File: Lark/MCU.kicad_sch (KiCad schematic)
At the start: 19 parts, among them J9 0530470410, U14 STM32H743VIT6, Y1 8Mhz

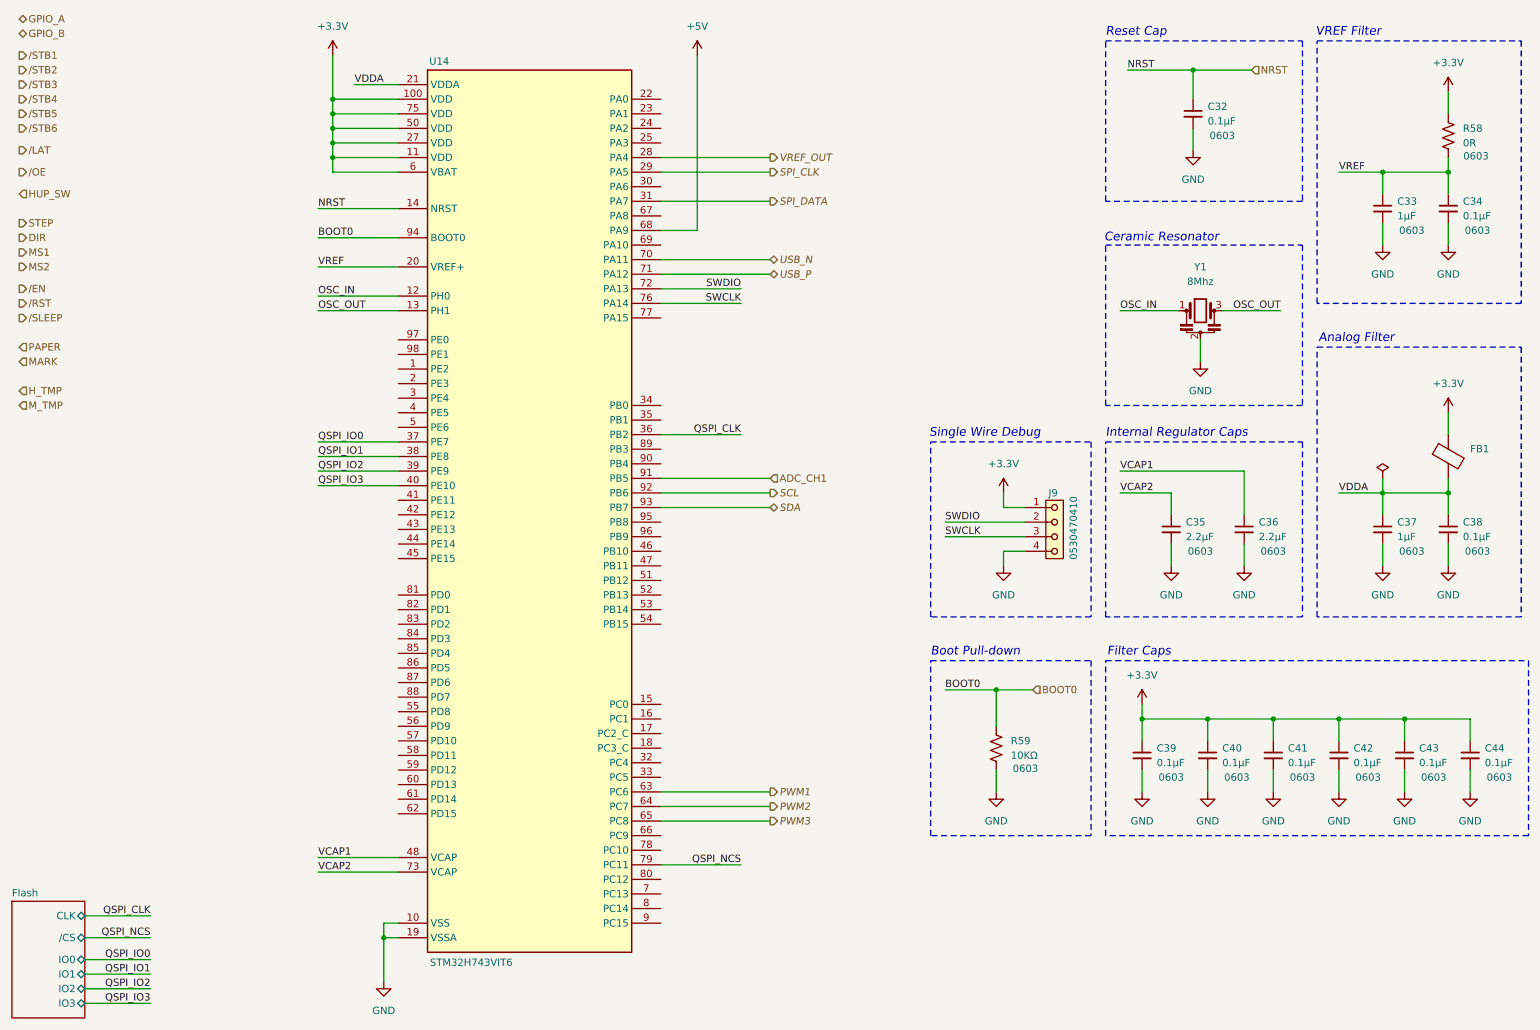
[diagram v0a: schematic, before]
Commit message: updated WIP
- fixed high-side switch (swapped out pfets)
- swapped out bleeder fet.
- changed a few footprints.
- changed zeners to 15v ones
- added soft-start cap back in to the high-side switch.

(today ive mainly been struggling with the inrush current, but I think its solved now)
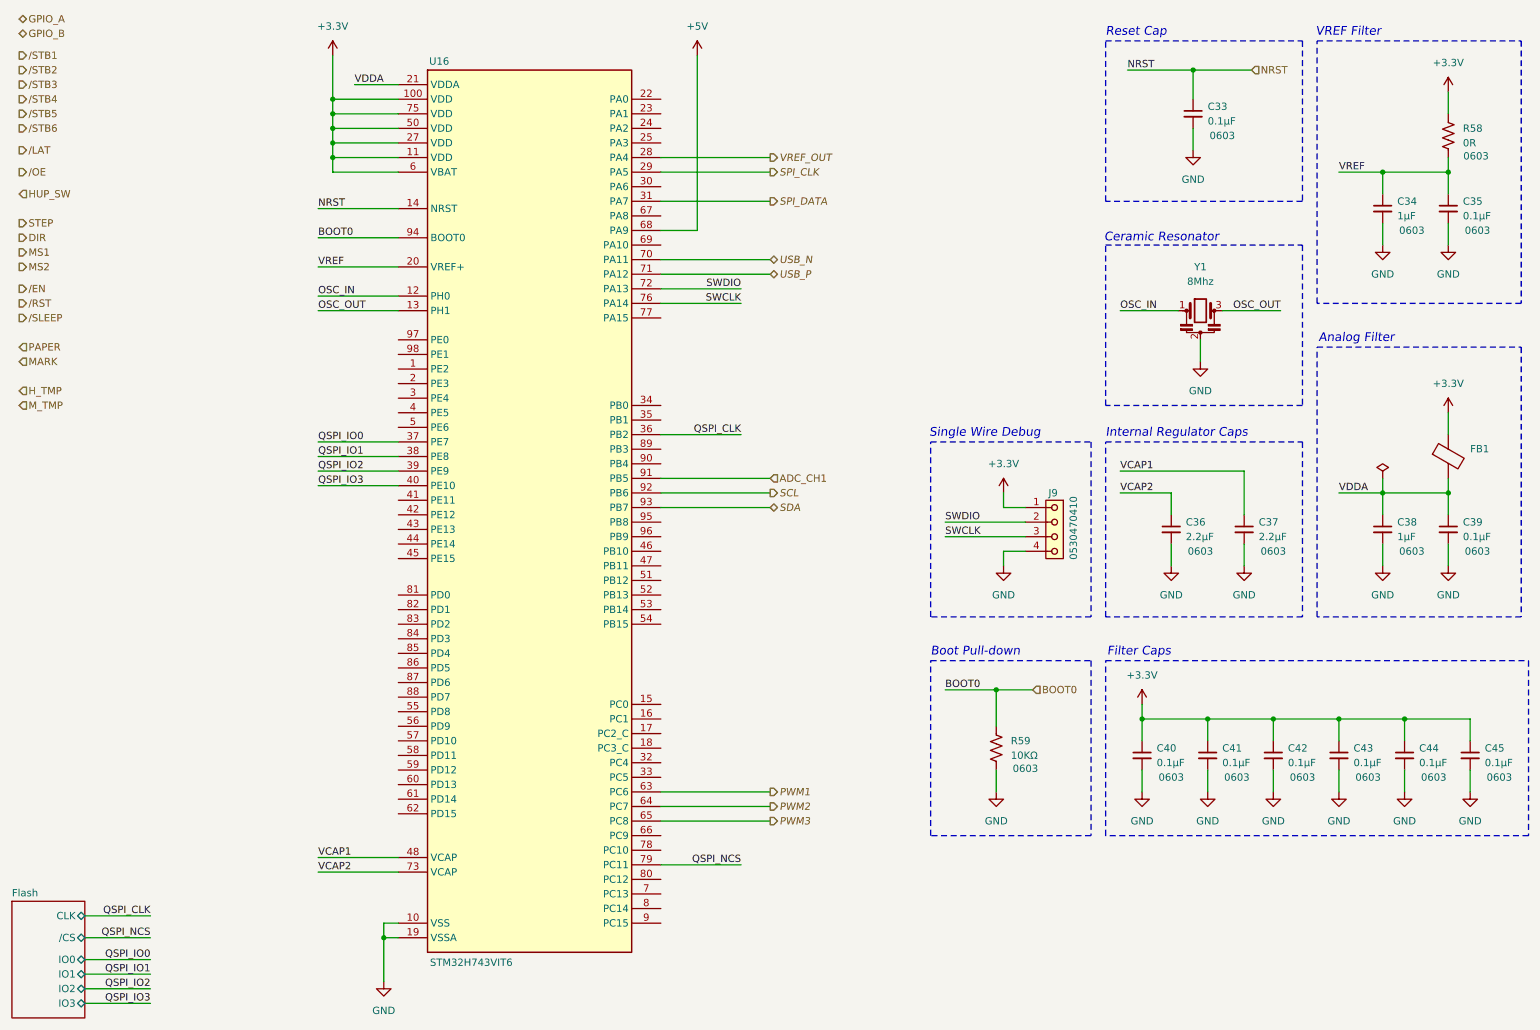
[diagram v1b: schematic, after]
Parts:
- renumbered C32 to C33, C33 to C34, C34 to C35, C35 to C36, C36 to C37, C37 to C38, C38 to C39, C39 to C40, C40 to C41, C41 to C42, C42 to C43, C43 to C44, C44 to C45, U14 to U16

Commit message: updated layout
got all the control signals routed finally.
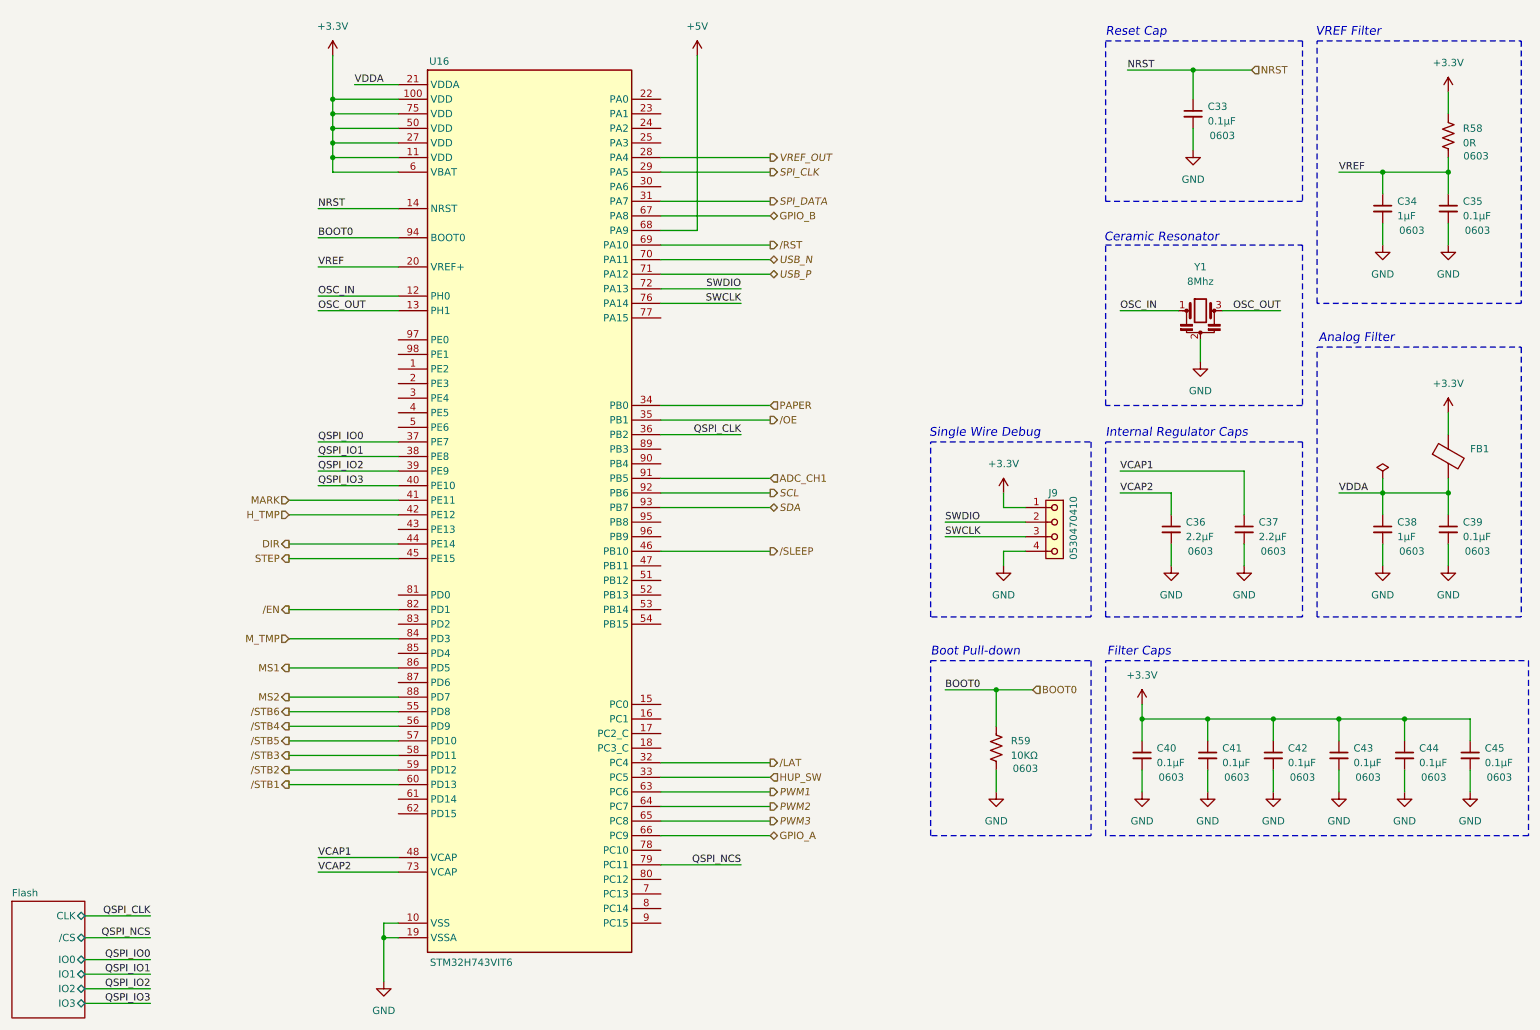
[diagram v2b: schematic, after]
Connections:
- net DIR: now also U16.44 (PE14)
- net GPIO_A: now also U16.66 (PC9)
- net GPIO_B: now also U16.67 (PA8)
- net HUP_SW: now also U16.33 (PC5)
- net H_TMP: now also U16.42 (PE12)
- net MARK: now also U16.41 (PE11)
- net MS1: now also U16.86 (PD5)
- net MS2: now also U16.88 (PD7)
- net M_TMP: now also U16.84 (PD3)
- net PAPER: now also U16.34 (PB0)
- net STEP: now also U16.45 (PE15)
- net /EN: now also U16.82 (PD1)
- net /LAT: now also U16.32 (PC4)
- net /OE: now also U16.35 (PB1)
- net /RST: now also U16.69 (PA10)
- net /SLEEP: now also U16.46 (PB10)
- net /STB1: now also U16.60 (PD13)
- net /STB2: now also U16.59 (PD12)
- net /STB3: now also U16.58 (PD11)
- net /STB4: now also U16.56 (PD9)
- net /STB5: now also U16.57 (PD10)
- net /STB6: now also U16.55 (PD8)

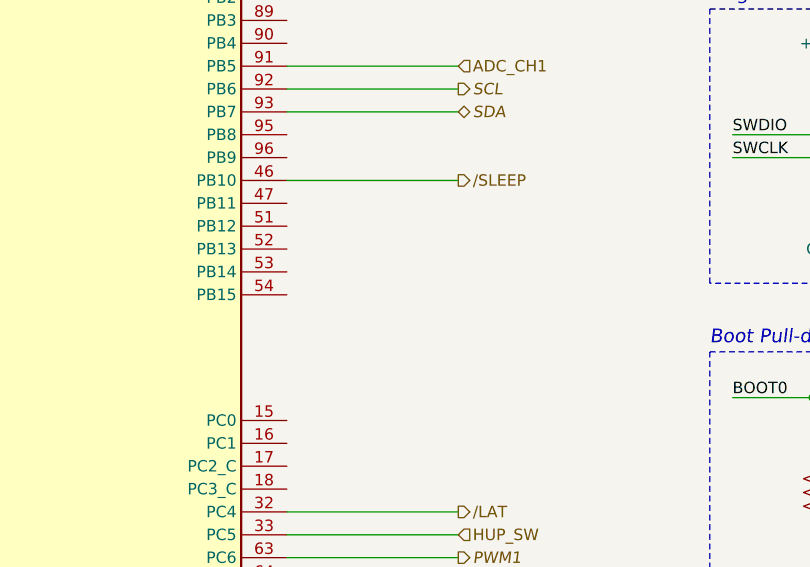
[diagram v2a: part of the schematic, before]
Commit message: The right side of the board is finalized.
- Finalized the logic side of the board (right)
- Will work on the power section next.
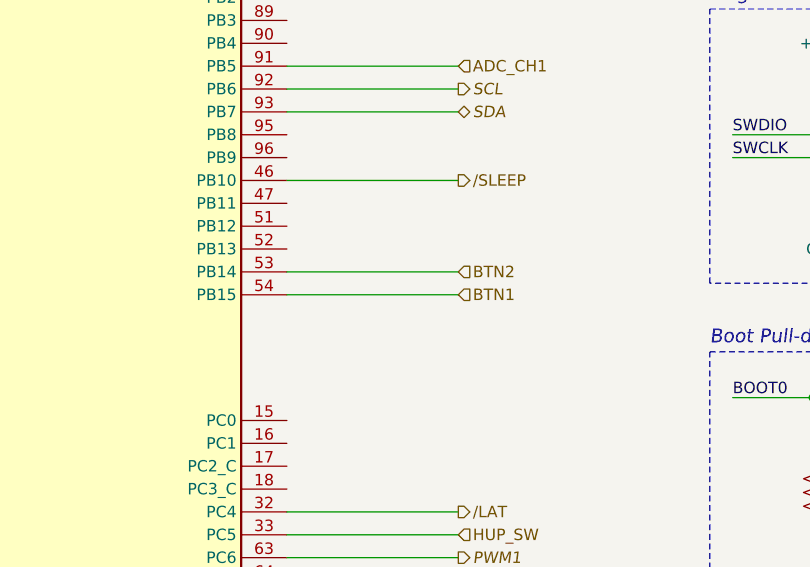
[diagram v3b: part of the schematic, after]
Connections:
- net BTN2: now reaches U16.53 (PB14)
- net BTN1: now reaches U16.54 (PB15)
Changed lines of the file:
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@@
+	(wire
+		(pts
+			(xy 130.81 120.65) (xy 149.86 120.65)
+		)
+		(stroke
+			(width 0)
+			(type default)
+		)
+	)
 	(wire
 		(pts
@@
 		(pts
 			(xy 66.04 109.22) (xy 85.09 109.22)
+		)
+		(stroke
+			(width 0)
+			(type default)
+		)
+	)
+	(wire
+		(pts
+			(xy 130.81 123.19) (xy 149.86 123.19)
 		)
 		(stroke
@@
 		)
 	)
+	(hierarchical_label "BTN2"
+		(shape input)
+		(at 149.86 120.65 0)
+		(effects
+			(font
+				(size 1.27 1.27)
+			)
+			(justify left)
+		)
+	)
 	(hierarchical_label "PAPER"
 		(shape input)
@@
 		)
 	)
+	(hierarchical_label "BTN1"
+		(shape input)
+		(at 149.86 123.19 0)
+		(effects
+			(font
+				(size 1.27 1.27)
+			)
+			(justify left)
+		)
+	)

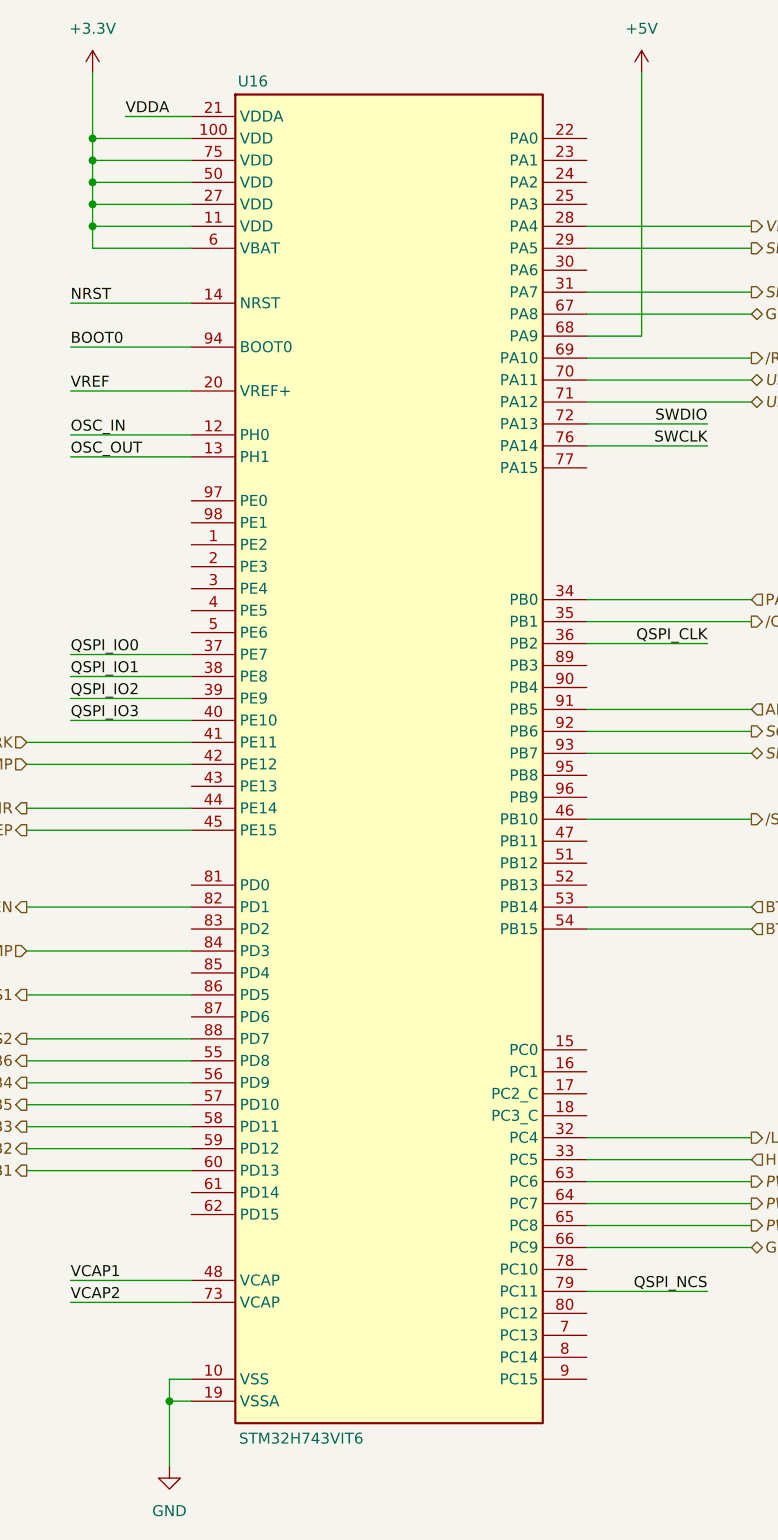
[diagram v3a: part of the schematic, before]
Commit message: minor updates
- changed npn pins to passive.
- changed rev to match working revision.
- minor PCB changes.
- moved TVS diode next to connector.
- changed barrel jack silkscreen.
- changed usbc silkscreen.
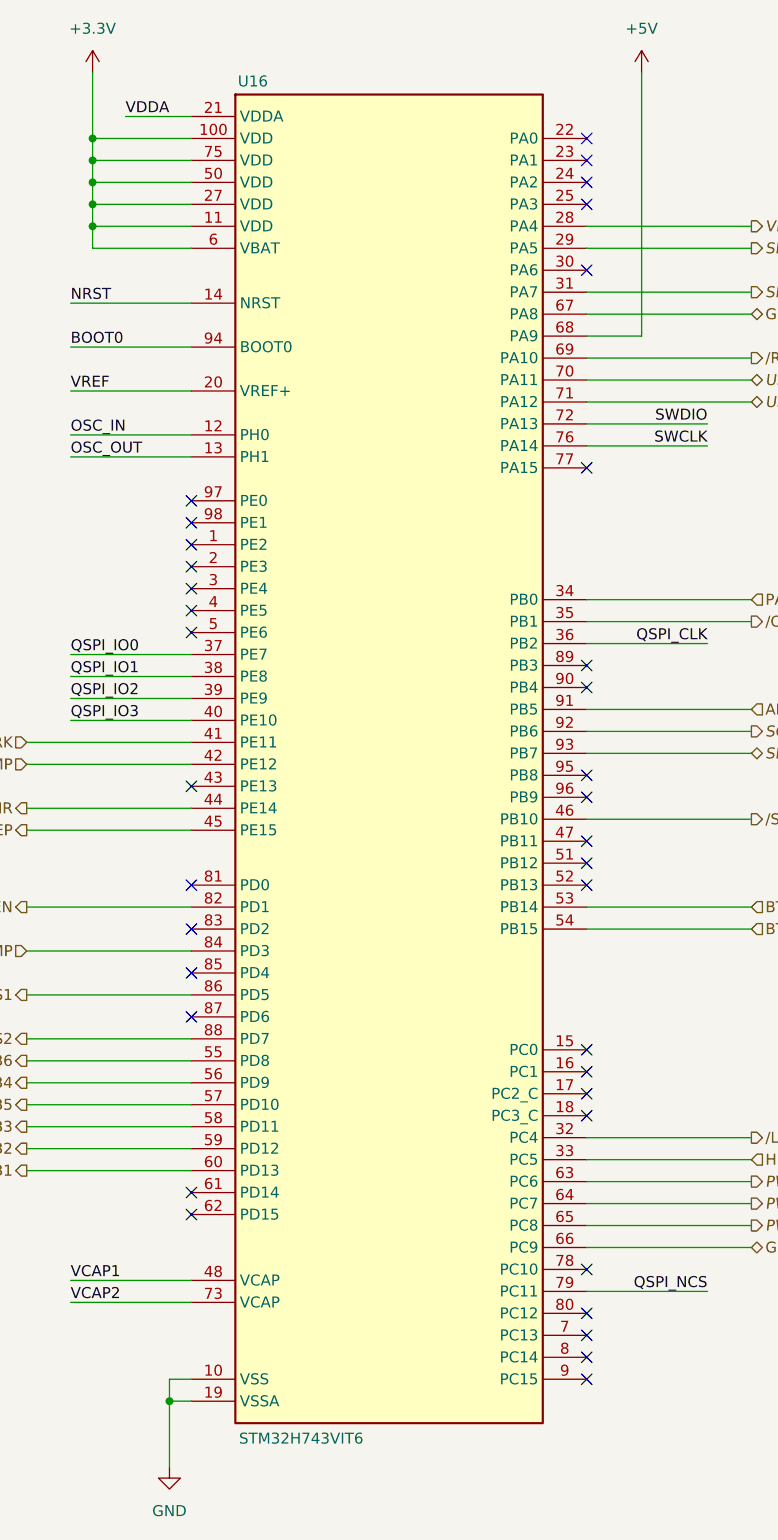
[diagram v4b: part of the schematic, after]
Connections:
- no-connect marks 0 -> 36
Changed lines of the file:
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@@
 		(title "Lark Print Engine")
 		(date "2025-10-08")
-		(rev "01.00.01")
+		(rev "01.00.00")
 		(comment 1 "Thermal Print Engine")
 		(comment 2 "Designer: HamSlices")
@@
 		(color 0 0 0 0)
 	)
+	(no_connect
+		(at 130.81 172.72)
+	)
+	(no_connect
+		(at 85.09 81.28)
+	)
+	(no_connect
+		(at 85.09 76.2)
+	)
+	(no_connect
+		(at 85.09 123.19)
+	)
+	(no_connect
+		(at 130.81 142.24)
+	)
+	(no_connect
+		(at 130.81 92.71)
+	)
+	(no_connect
+		(at 85.09 118.11)
+	)
+	(no_connect
+		(at 85.09 78.74)
+	)
+	(no_connect
+		(at 130.81 46.99)
+	)
+	(no_connect
+		(at 85.09 153.67)
+	)
+	(no_connect
+		(at 130.81 144.78)
+	)
+	(no_connect
+		(at 85.09 156.21)
+	)
+	(no_connect
+		(at 85.09 86.36)
+	)
+	(no_connect
+		(at 130.81 31.75)
+	)
+	(no_connect
+		(at 130.81 118.11)
+	)
+	(no_connect
+		(at 130.81 115.57)
+	)
+	(no_connect
+		(at 130.81 175.26)
+	)
+	(no_connect
+		(at 85.09 83.82)
+	)
+	(no_connect
+		(at 130.81 170.18)
+	)
+	(no_connect
+		(at 130.81 139.7)
+	)
+	(no_connect
+		(at 130.81 167.64)
+	)
+	(no_connect
+		(at 85.09 128.27)
+	)
+	(no_connect
+		(at 130.81 107.95)
+	)
+	(no_connect
+		(at 130.81 36.83)
+	)
+	(no_connect
+		(at 85.09 88.9)
+	)
+	(no_connect
+		(at 130.81 105.41)
+	)
+	(no_connect
+		(at 130.81 137.16)
+	)
+	(no_connect
+		(at 85.09 106.68)
+	)
+	(no_connect
+		(at 130.81 39.37)
+	)
+	(no_connect
+		(at 85.09 73.66)
+	)
+	(no_connect
+		(at 130.81 34.29)
+	)
+	(no_connect
+		(at 130.81 113.03)
+	)
+	(no_connect
+		(at 85.09 133.35)
+	)
+	(no_connect
+		(at 130.81 95.25)
+	)
+	(no_connect
+		(at 130.81 69.85)
+	)
+	(no_connect
+		(at 130.81 162.56)
+	)
 	(wire
